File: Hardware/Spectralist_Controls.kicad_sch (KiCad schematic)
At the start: 27 parts, among them J1 Conn_01x12_Male, J10 FilterA_CV, J11 FilterB_CV, J12 ChannelAOut, J13 ChannelBOut, J14 StretchCV, J2 Conn_01x12_Male, J3 Conn_01x16_Male, J4 Conn_01x16_Male, J5 StretchCV, J6 VOctCV, J7 WarpCV, J8 PanCV, SW1 Harmonic_Switch, SW2 Filter_Switch, SW3 B_Octave

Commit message: Updates to LED board
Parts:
- SW1: footprint Custom_Footprints:SPDT_Miniature -> Custom_Footprints:SPDT_SubMiniature_Aligned
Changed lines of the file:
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@@
 			)
 		)
-		(property "Footprint" "Custom_Footprints:SPDT_Miniature"
+		(property "Footprint" "Custom_Footprints:SPDT_SubMiniature_Aligned"
 			(at 38.1 167.64 0)
 			(effects

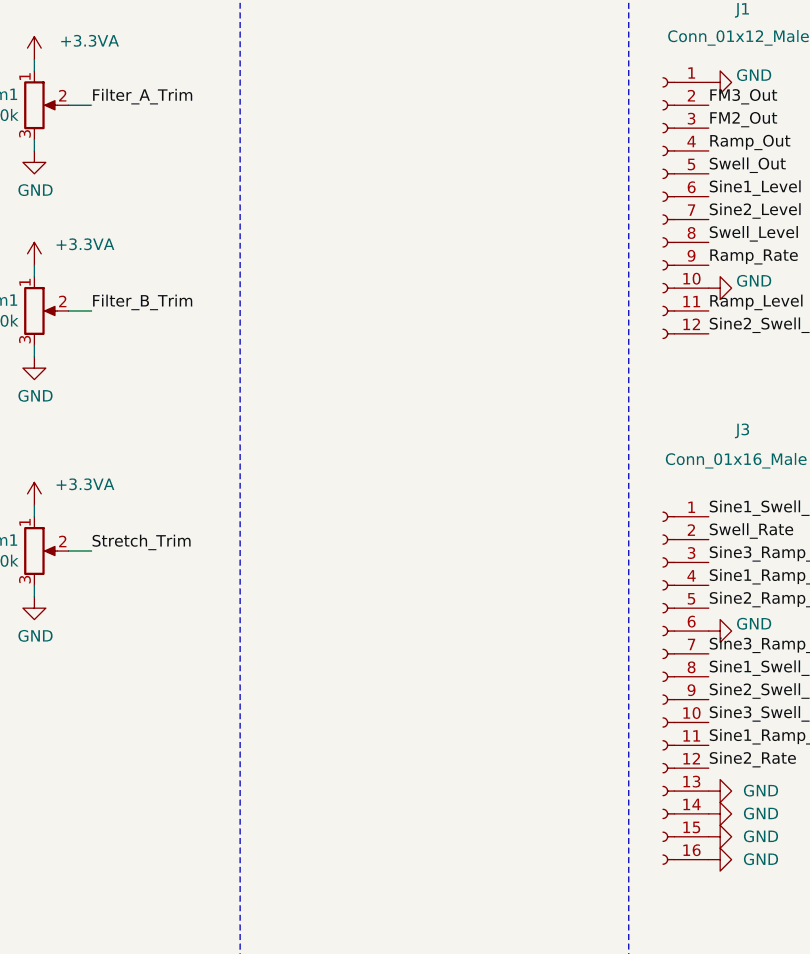
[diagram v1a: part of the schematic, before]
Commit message: Curvy traces on LED board
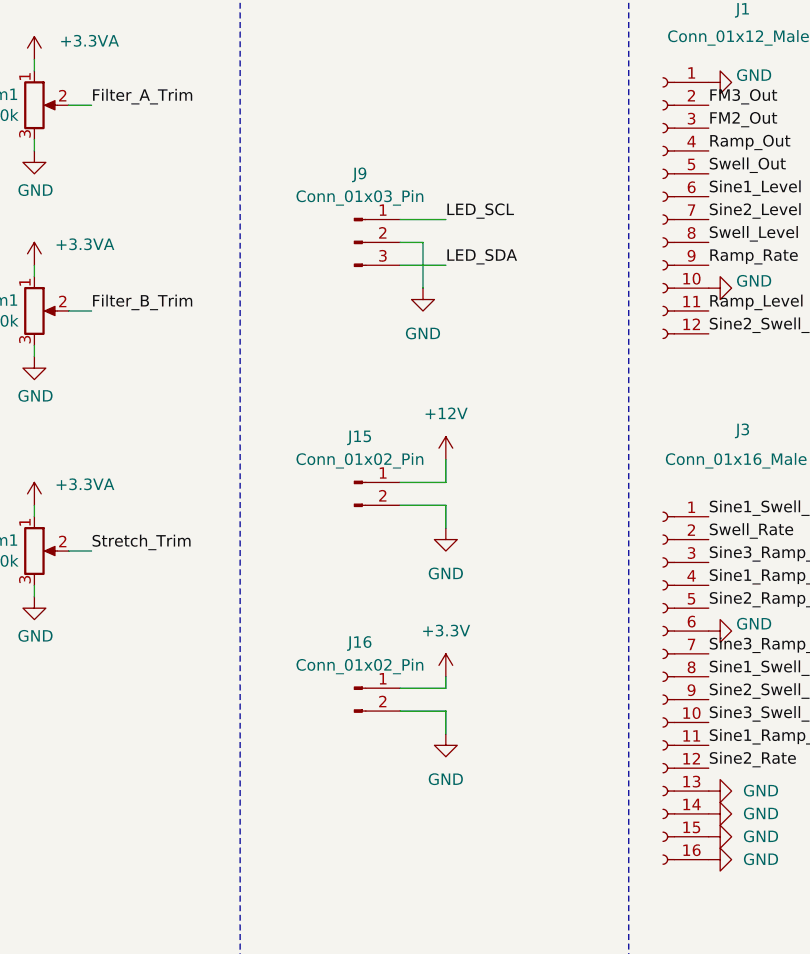
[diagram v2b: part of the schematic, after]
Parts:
- added J15, J16: Conn_01x02_Pin, Connector_PinHeader_2.54mm:PinHeader_1x02_P2.54mm_Vertical, symbol Connector:Conn_01x02_Pin
- added J9: Conn_01x03_Pin, Connector_PinHeader_2.54mm:PinHeader_1x03_P2.54mm_Vertical, symbol Connector:Conn_01x03_Pin
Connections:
- net +3.3V: now also J16.1 (Pin_1)
- net GND: now also J15.2 (Pin_2), J16.2 (Pin_2), J9.2 (Pin_2)
- new net +12V: J15.1 (Pin_1)
- new net LED_SCL: J9.1 (Pin_1)
- new net LED_SDA: J9.3 (Pin_3)

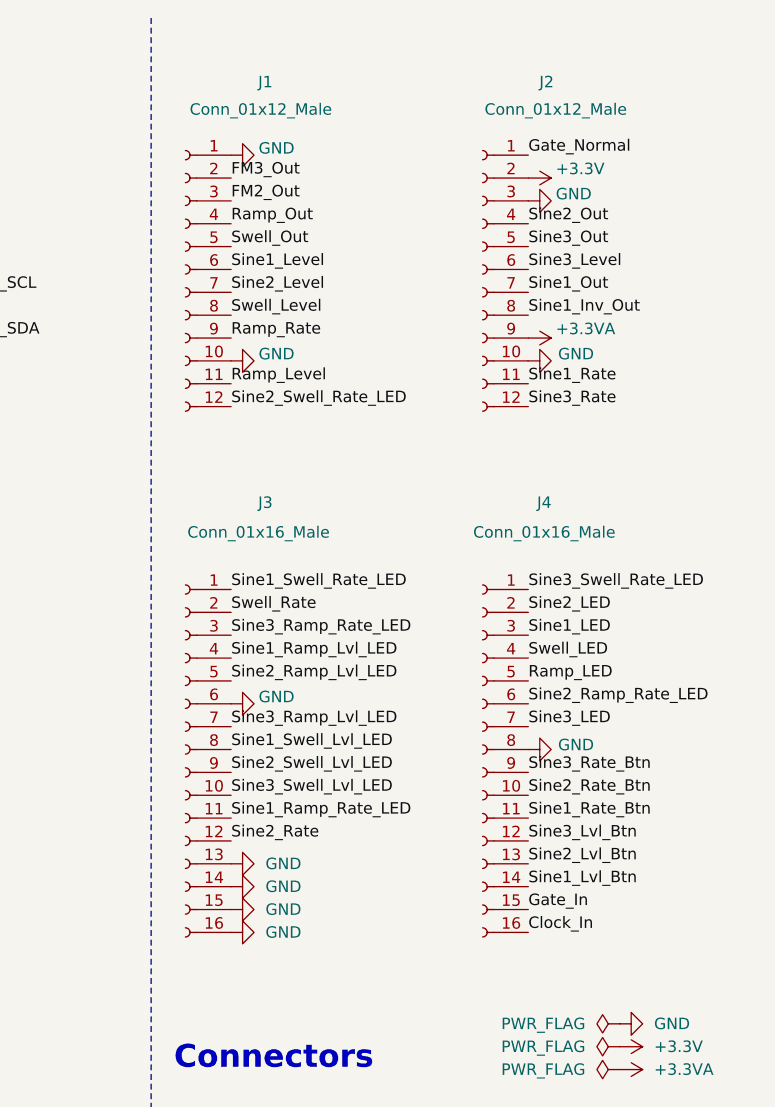
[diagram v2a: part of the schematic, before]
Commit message: Component PCB updates
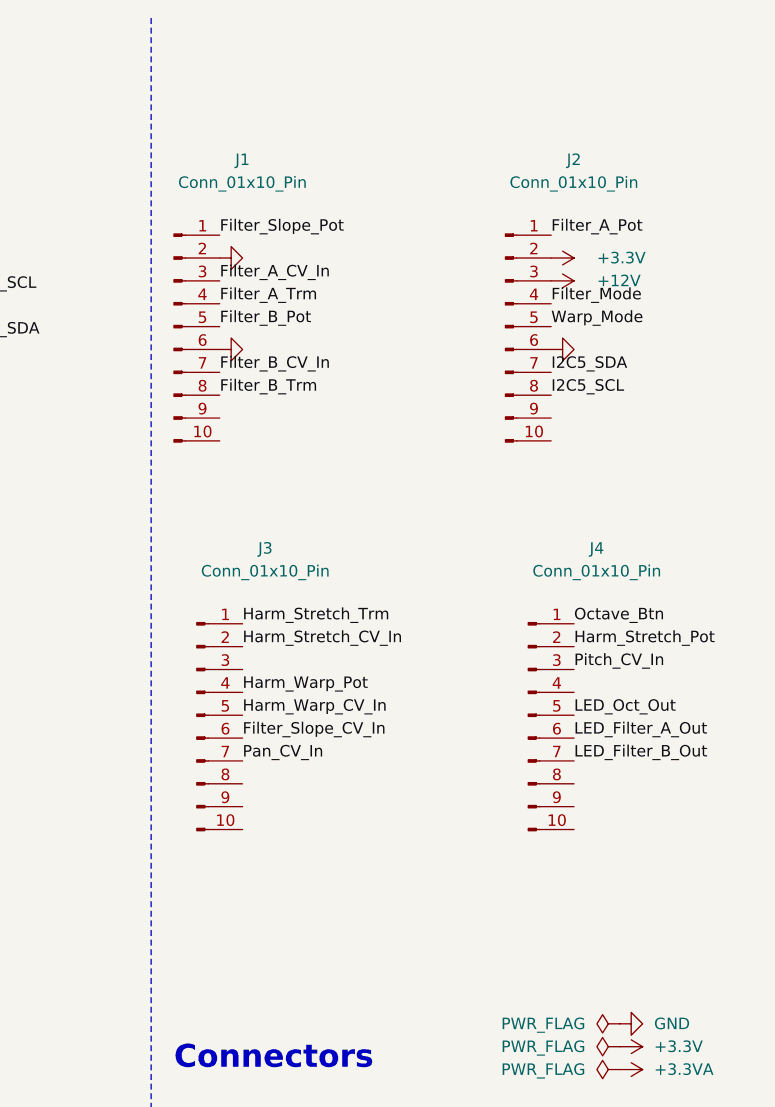
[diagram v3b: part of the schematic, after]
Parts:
- removed J1, J2: Conn_01x12_Male, Connector_PinSocket_2.54mm:PinSocket_1x12_P2.54mm_Vertical, symbol Connector:Conn_01x12_Socket
- removed J3, J4: Conn_01x16_Male, Connector_PinSocket_2.54mm:PinSocket_1x16_P2.54mm_Vertical, symbol Connector:Conn_01x16_Socket
- added J1, J2, J3, J4: Conn_01x10_Pin, Connector_PinHeader_2.54mm:PinHeader_1x10_P2.54mm_Vertical, symbol Connector:Conn_01x10_Pin
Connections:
- net +12V: now also J2.3 (Pin_3)
- net +3.3V: now also J2.2 (Pin_2)
- net GND: now also J1.2 (Pin_2), J1.6 (Pin_6), J2.6 (Pin_6)
- net Octave_Btn: now also J4.1 (Pin_1)
- new net Filter_A_CV_In: J1.3 (Pin_3)
- new net Filter_A_Pot: J2.1 (Pin_1)
- new net Filter_A_Trm: J1.4 (Pin_4)
- new net Filter_B_CV_In: J1.7 (Pin_7)
- new net Filter_B_Pot: J1.5 (Pin_5)
- new net Filter_B_Trm: J1.8 (Pin_8)
- new net Filter_Mode: J2.4 (Pin_4)
- new net Filter_Slope_CV_In: J3.6 (Pin_6)
- new net Filter_Slope_Pot: J1.1 (Pin_1)
- new net Harm_Stretch_CV_In: J3.2 (Pin_2)
- new net Harm_Stretch_Pot: J4.2 (Pin_2)
- new net Harm_Stretch_Trm: J3.1 (Pin_1)
- new net Harm_Warp_CV_In: J3.5 (Pin_5)
- new net Harm_Warp_Pot: J3.4 (Pin_4)
- new net I2C5_SCL: J2.8 (Pin_8)
- new net I2C5_SDA: J2.7 (Pin_7)
- new net LED_Filter_A_Out: J4.6 (Pin_6)
- new net LED_Filter_B_Out: J4.7 (Pin_7)
- new net LED_Oct_Out: J4.5 (Pin_5)
- new net Pan_CV_In: J3.7 (Pin_7)
- new net Pitch_CV_In: J4.3 (Pin_3)
- new net Warp_Mode: J2.5 (Pin_5)

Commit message: More layout on Component and Control boards
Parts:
- removed J1, J2: Conn_01x10_Pin, Connector_PinHeader_2.54mm:PinHeader_1x10_P2.54mm_Vertical, symbol Connector:Conn_01x10_Pin
- added J1, J2: Conn_01x8_Pin, Connector_PinHeader_2.54mm:PinHeader_1x08_P2.54mm_Vertical, symbol Connector:Conn_01x08_Pin
- J14: value StretchCV -> SlopeCV
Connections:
- net Filter_A_Cutoff is gone; now on net Filter_A_Pot: Filter_A_Cutoff1.2
- net Filter_A_In is gone; now on net Filter_A_CV_In: J10.3
- net Filter_A_LED is gone; now on net LED_Filter_A_Out: D1.2 (A)
- net Filter_A_Trim is gone; now on net Filter_A_Trm: Filter_A_Trim1.2
- net Filter_B_Cutoff is gone; now on net Filter_B_Pot: Filter_B_Cutoff1.2
- net Filter_B_In is gone; now on net Filter_B_CV_In: J11.3
- net Filter_B_LED is gone; now on net LED_Filter_B_Out: D2.2 (A)
- net Filter_B_Trim is gone; now on net Filter_B_Trm: Filter_B_Trim1.2
- net Filter_Slope is gone; now on net Filter_Slope_Pot: Filter_Slope_Pot1.2
- net Filter_Type is gone; now on net Filter_Mode: SW2.2 (B)
- net Harmonic_Stretch is gone; now on net Harm_Stretch_Pot: Harmonic_Stretch_Pot1.2
- net Harmonic_Warp is gone; now on net Harm_Warp_Pot: Harmonic_Warp_Pot1.2
- net Octave_LED is gone; now on net LED_Oct_Out: D3.2 (A)
- net Pan_In is gone; now on net Pan_CV_In: J8.3
- net Stretch_Trim is gone; now on net Harm_Stretch_Trm: Stretch_Trim1.2
- net V_Oct_In is gone; now on net Pitch_CV_In: J6.3
- net Warp_In is gone; now on net Harm_Warp_CV_In: J7.3
- net +12V: now also J2.8 (Pin_8)
- net +3.3V: now also J2.1 (Pin_1)
- net Filter_A_CV_In: now also J4.10 (Pin_10)
- net Filter_A_Pot: now also J2.6 (Pin_6)
- net Filter_A_Trm: now also J2.7 (Pin_7)
- net Filter_B_CV_In: now also J4.3 (Pin_3)
- net Filter_B_Pot: now also J3.6 (Pin_6)
- net Filter_B_Trm: now also J3.1 (Pin_1)
- net Filter_Mode: now also J2.2 (Pin_2)
- net Filter_Slope_CV_In: now also J14.3, J4.5 (Pin_5); no longer J3.6 (Pin_6)
- net Filter_Slope_Pot: now also J3.5 (Pin_5)
- net GND: now also J3.3 (Pin_3), J3.7 (Pin_7), J4.1 (Pin_1), J4.4 (Pin_4), J4.7 (Pin_7), J1.1 (Pin_1), J1.4 (Pin_4), J1.7 (Pin_7), J2.4 (Pin_4)
- net Harm_Stretch_CV_In: now also J4.9 (Pin_9), J5.3; no longer J3.2 (Pin_2)
- net Harm_Stretch_Pot: now also J3.9 (Pin_9); no longer J4.2 (Pin_2)
- net Harm_Stretch_Trm: now also J3.8 (Pin_8); no longer J3.1 (Pin_1)
- net Harm_Warp_CV_In: now also J4.2 (Pin_2); no longer J3.5 (Pin_5)
- net Harm_Warp_Pot: now also J3.10 (Pin_10); no longer J3.4 (Pin_4)
- net Harmonic_Mode: now also J2.3 (Pin_3)
- net LED_Filter_A_Out: now also J1.5 (Pin_5); no longer J4.6 (Pin_6)
- net LED_Filter_B_Out: now also J1.8 (Pin_8); no longer J4.7 (Pin_7)
- net LED_Oct_Out: now also J1.6 (Pin_6); no longer J4.5 (Pin_5)
- net LED_SCL: now also J1.2 (Pin_2)
- net LED_SDA: now also J1.3 (Pin_3)
- net Octave_Btn: now also J2.5 (Pin_5); no longer J4.1 (Pin_1)
- net Pan_CV_In: now also J4.6 (Pin_6); no longer J3.7 (Pin_7)
- net Pitch_CV_In: now also J4.8 (Pin_8); no longer J4.3 (Pin_3)
- net Channel_A_Out renamed Audio_Out_L
- net Audio_Out_L: now also J3.2 (Pin_2)
- net Channel_B_Out renamed Audio_Out_R
- net Audio_Out_R: now also J3.4 (Pin_4)
- removed net Stretch_In: J14.3, J5.3

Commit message: More PCB Layout
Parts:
- renumbered Filter_B_Trim1 to Filter_B_Cutoff1, Filter_B_Cutoff1 to Filter_B_Trim1
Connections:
- net Filter_B_Pot: now also Filter_B_Cutoff1.2, J3.1 (Pin_1); no longer Filter_B_Trim1.2, J3.6 (Pin_6)
- net Filter_B_Trm: now also Filter_B_Trim1.2, J3.6 (Pin_6); no longer Filter_B_Cutoff1.2, J3.1 (Pin_1)
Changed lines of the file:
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@@
 	)
 	(label "Filter_B_Trm"
-		(at 228.6 78.74 0)
+		(at 228.6 91.44 0)
 		(fields_autoplaced yes)
 		(effects
@@
 	)
 	(label "Filter_B_Pot"
-		(at 228.6 91.44 0)
+		(at 228.6 78.74 0)
 		(fields_autoplaced yes)
 		(effects
@@
 	)
 	(label "Filter_B_Pot"
-		(at 115.57 52.07 0)
+		(at 160.02 53.34 0)
 		(fields_autoplaced yes)
 		(effects
@@
 	)
 	(label "Filter_B_Trm"
-		(at 160.02 53.34 0)
+		(at 115.57 52.07 0)
 		(fields_autoplaced yes)
 		(effects
@@
 		(on_board yes)
 		(dnp no)
-		(property "Reference" "Filter_B_Cutoff1"
+		(property "Reference" "Filter_B_Trim1"
 			(at 107.4674 50.9016 0)
 			(effects
@@
 			(project "Kishoof_Controls"
 				(path "/00778401-a8b8-4a7c-bae7-c4fa7505df01"
-					(reference "Filter_B_Cutoff1")
+					(reference "Filter_B_Trim1")
 					(unit 1)
 				)
@@
 		(on_board yes)
 		(dnp no)
-		(property "Reference" "Filter_B_Trim1"
+		(property "Reference" "Filter_B_Cutoff1"
 			(at 151.9174 52.1716 0)
 			(effects
@@
 			(project "Spectralist_Controls"
 				(path "/00778401-a8b8-4a7c-bae7-c4fa7505df01"
-					(reference "Filter_B_Trim1")
+					(reference "Filter_B_Cutoff1")
 					(unit 1)
 				)

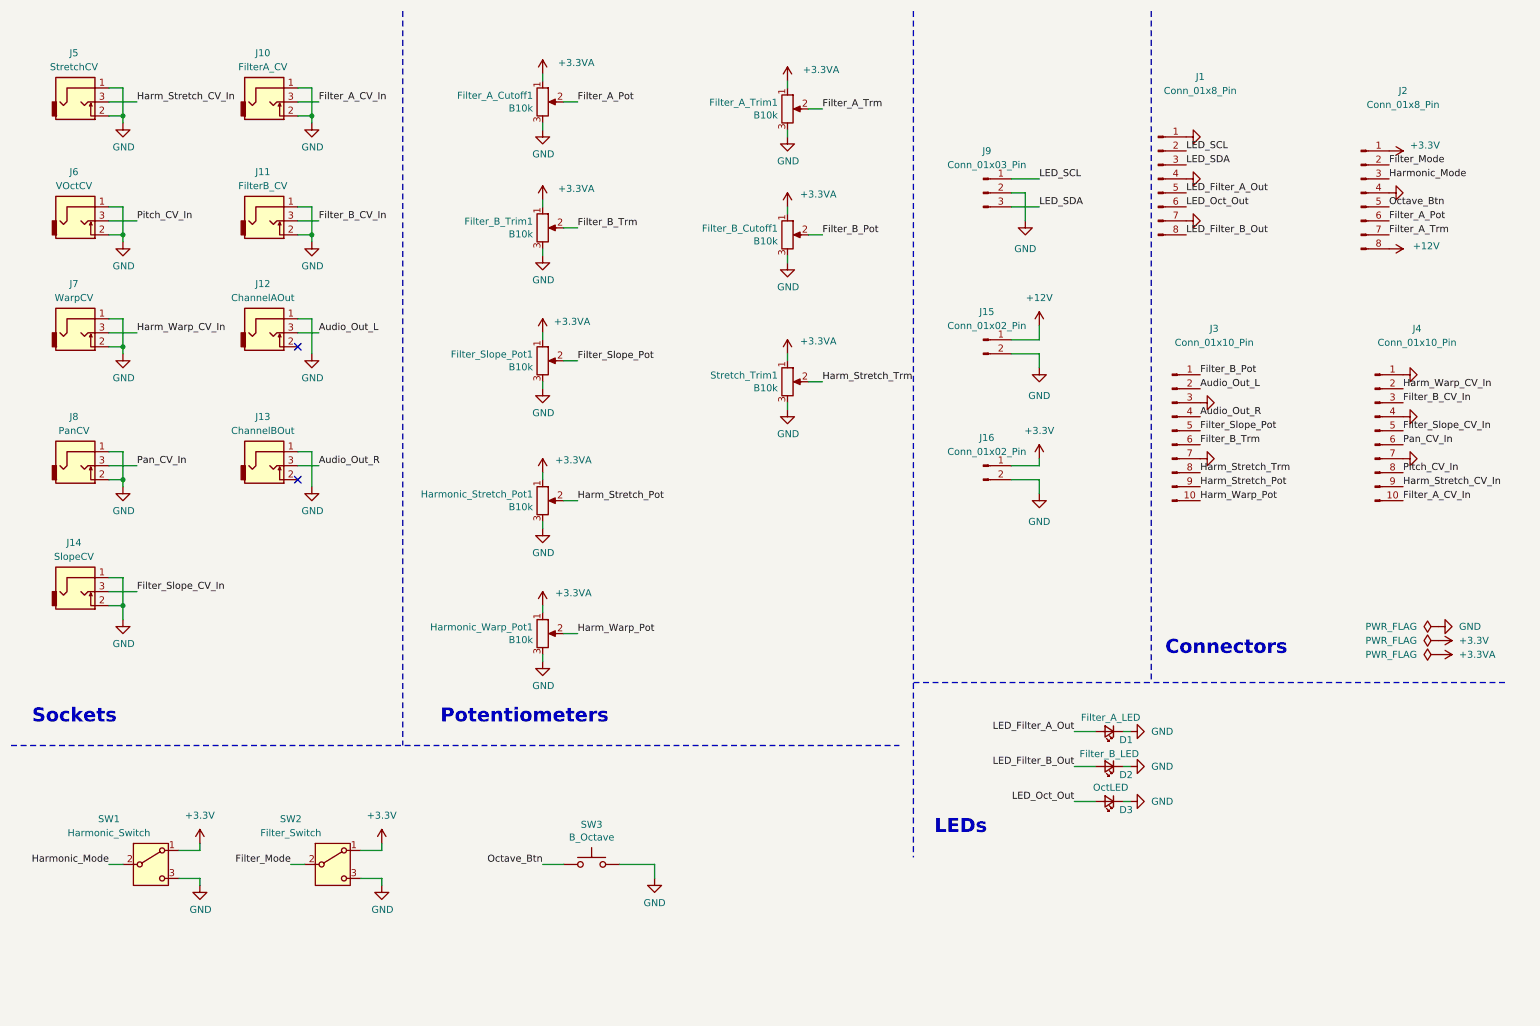
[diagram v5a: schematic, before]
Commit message: Started adding JLC part numbers
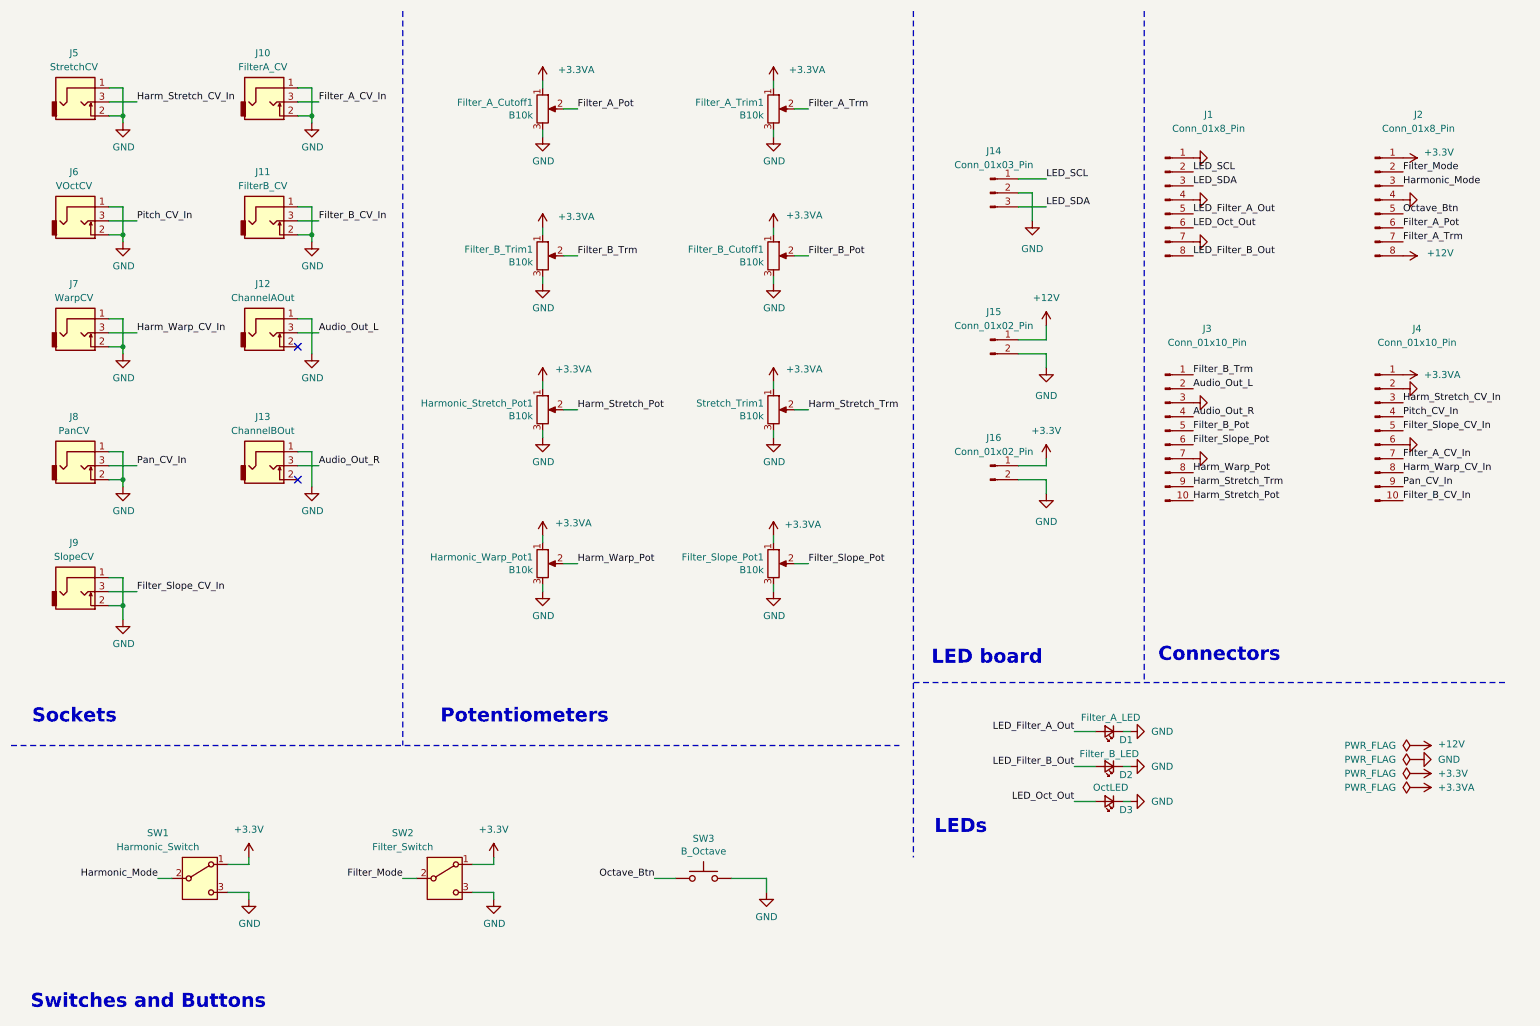
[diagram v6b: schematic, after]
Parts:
- J1, J2: footprint Connector_PinHeader_2.54mm:PinHeader_1x08_P2.54mm_Vertical -> Connector_PinSocket_2.54mm:PinSocket_1x08_P2.54mm_Vertical
- J3, J4: footprint Connector_PinHeader_2.54mm:PinHeader_1x10_P2.54mm_Vertical -> Connector_PinSocket_2.54mm:PinSocket_1x10_P2.54mm_Vertical
- renumbered J9 to J14, J14 to J9
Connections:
- net +3.3VA: now also J4.1 (Pin_1)
- net Filter_A_CV_In: now also J4.7 (Pin_7); no longer J4.10 (Pin_10)
- net Filter_B_CV_In: now also J4.10 (Pin_10); no longer J4.3 (Pin_3)
- net Filter_B_Pot: now also J3.5 (Pin_5); no longer J3.1 (Pin_1)
- net Filter_B_Trm: now also J3.1 (Pin_1); no longer J3.6 (Pin_6)
- net Filter_Slope_Pot: now also J3.6 (Pin_6); no longer J3.5 (Pin_5)
- net GND: now also J4.2 (Pin_2), J4.6 (Pin_6); no longer J4.1 (Pin_1), J4.4 (Pin_4), J4.7 (Pin_7)
- net Harm_Stretch_CV_In: now also J4.3 (Pin_3); no longer J4.9 (Pin_9)
- net Harm_Stretch_Pot: now also J3.10 (Pin_10); no longer J3.9 (Pin_9)
- net Harm_Stretch_Trm: now also J3.9 (Pin_9); no longer J3.8 (Pin_8)
- net Harm_Warp_CV_In: now also J4.8 (Pin_8); no longer J4.2 (Pin_2)
- net Harm_Warp_Pot: now also J3.8 (Pin_8); no longer J3.10 (Pin_10)
- net Pan_CV_In: now also J4.9 (Pin_9); no longer J4.6 (Pin_6)
- net Pitch_CV_In: now also J4.4 (Pin_4); no longer J4.8 (Pin_8)
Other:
- note added: "LED board"
- note added: "Switches and Buttons"
- moved on the sheet: Filter_A_Cutoff1, Filter_A_Trim1, Filter_B_Cutoff1, Filter_B_Trim1, Filter_Slope_Pot1, Harmonic_Stretch_Pot1, Harmonic_Warp_Pot1, J1, J14, J15, J16, J2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
